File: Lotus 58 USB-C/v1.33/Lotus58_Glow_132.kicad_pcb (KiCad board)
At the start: 2 copper layers, 139.1 x 107.7 mm, 117 parts, among them J3 USB_C_Receptacle_USB2.0, P1 OLED, SW1 Kailh hotswap MX socket, SW10 Kailh hotswap MX socket, SW11 Kailh hotswap MX socket, SW12 Kailh hotswap MX socket, SW13 Kailh hotswap MX socket, SW14 Kailh hotswap MX socket, SW15 Kailh hotswap MX socket, SW16 Kailh hotswap MX socket, SW17 Kailh hotswap MX socket, SW18 Kailh hotswap MX socket, SW19 Kailh hotswap MX socket, SW2 Kailh hotswap MX socket, SW20 Kailh hotswap MX socket, SW21 Kailh hotswap MX socket, SW22 Kailh hotswap MX socket, SW23 Kailh hotswap MX socket, SW24 Kailh hotswap MX socket, SW25 Kailh hotswap MX socket, SW26 Kailh hotswap MX socket, SW27 Kailh hotswap MX socket, SW28 Kailh hotswap MX socket, SW29 Kailh hotswap MX socket, SW3 Kailh hotswap MX socket, SW30 Rotary_Encoder_Switch, SW31 Rotary_Encoder_Switch, SW32 MSK12C02, SW33 MSK12C02, SW4 Kailh hotswap MX socket, SW5 Kailh hotswap MX socket, SW6 Kailh hotswap MX socket, SW7 Kailh hotswap MX socket, SW8 Kailh hotswap MX socket, SW9 Kailh hotswap MX socket, U1 ProMicro, U2 SRV05-4

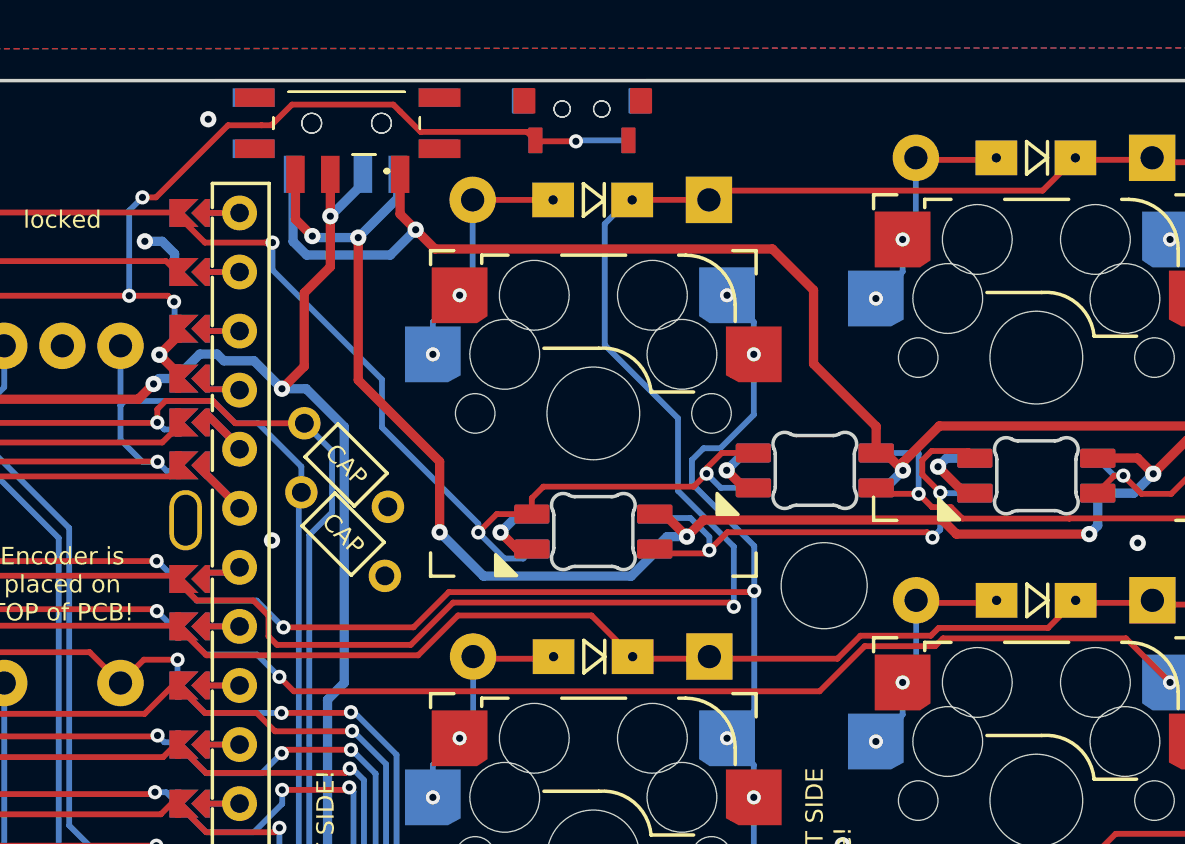
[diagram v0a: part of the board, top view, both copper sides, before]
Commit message: v1.32
Minor concessions for 3D printing
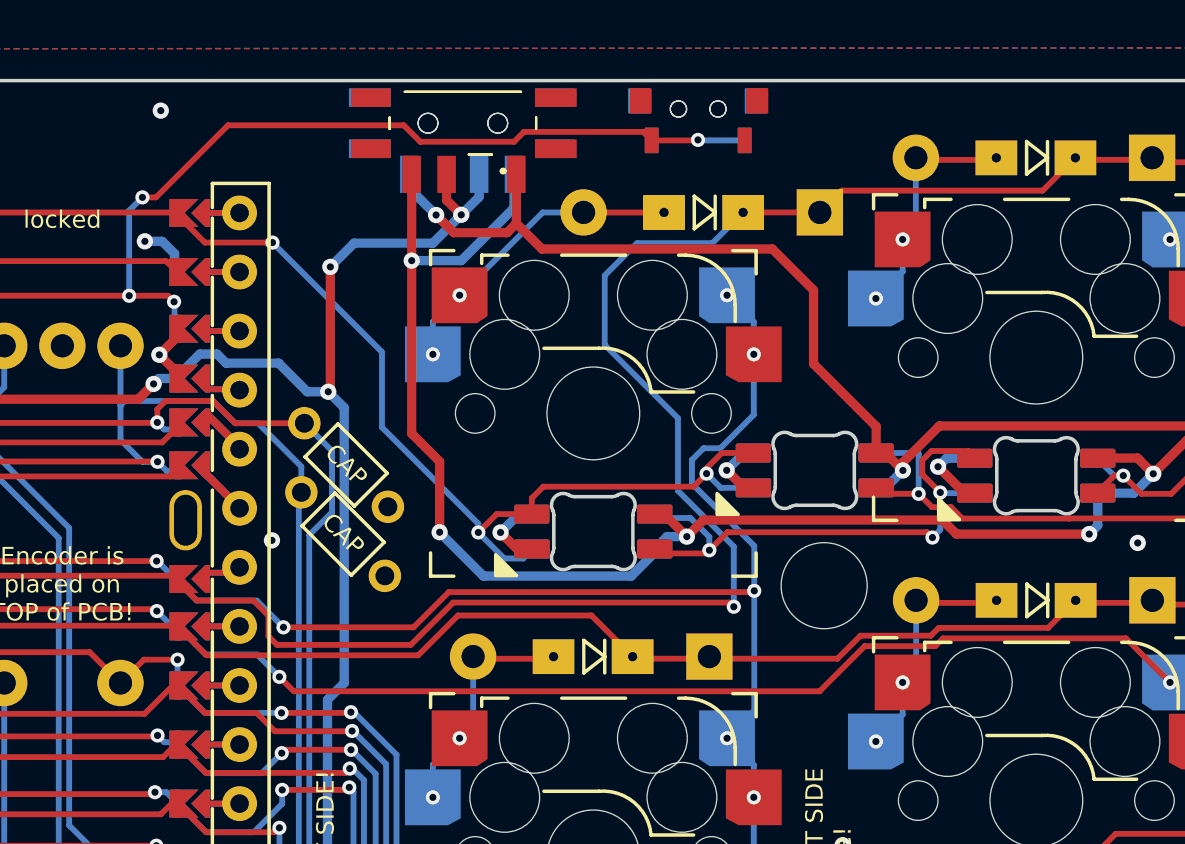
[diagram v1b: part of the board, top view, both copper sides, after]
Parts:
- moved RES1 5.00 mm to (118.9, 36.9)
- moved RES2 5.00 mm to (118.9, 36.9)
- moved SW32 5.00 mm to (108.8, 37.5)
- moved SW33 5.00 mm to (108.8, 37.5)
- moved D1 4.80 mm to (119.1, 41.4)
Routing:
- net /PWR_GLOW: track 314.1 -> 307.7 mm
- net VCC: track 84.6 -> 89.6 mm, vias 7 -> 8
- net RESET: track 39.8 -> 44.4 mm
- net Net-(D1-A): track 10.8 -> 13.4 mm
- net row0: track 162.4 -> 161.1 mm
- net /PWR_KEY: track 698.1 -> 699.2 mm, vias 37 -> 36
